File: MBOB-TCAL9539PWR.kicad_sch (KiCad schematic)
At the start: 1 part

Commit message: Finished drawing the schematics
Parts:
- added C1: 10u, symbol Device:C_Small
- added C2: 100n, symbol Device:C_Small
- added D1: LED, symbol Device:LED
- added H1, H2, H3, H4: MountingHole, symbol Mechanical:MountingHole
- added J1, J2: Conn_01x10, symbol Connector_Generic:Conn_01x10
- added J3, J4: QWIIC Right Angle, symbol Connector_Generic:Conn_01x04
- added J5: Conn_02x03_Odd_Even, symbol Connector_Generic:Conn_02x03_Odd_Even
- added JP1: SolderJumper_3_Open, symbol Jumper:SolderJumper_3_Open
- added JP2, JP3: SolderJumper_2_Open, symbol Jumper:SolderJumper_2_Open
- added R1, R2, R3, R4, R5, R6, R7: 4K7, symbol Device:R_Small
- U1: value ~ -> TCAL9539PWR; footprint (none) -> Package_SO:TSSOP-24_4.4x6.5mm_P0.5mm
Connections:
- net ~{INT}: now reaches U1.1 (~{INT})
- net ~{INT}: now also J5.5 (Pin_5), R2.2
- net P6: now reaches U1.10 (P6)
- net P6: now also J1.8 (Pin_8)
- net P7: now reaches U1.11 (P7)
- net P7: now also J1.9 (Pin_9)
- net P10: now reaches U1.13 (P10)
- net P10: now also J2.2 (Pin_2)
- net P11: now reaches U1.14 (P11)
- net P11: now also J2.3 (Pin_3)
- net P12: now reaches U1.15 (P12)
- net P12: now also J2.4 (Pin_4)
- net P13: now reaches U1.16 (P13)
- net P13: now also J2.5 (Pin_5)
- net P14: now reaches U1.17 (P14)
- net P14: now also J2.6 (Pin_6)
- net P15: now reaches U1.18 (P15)
- net P15: now also J2.7 (Pin_7)
- net P16: now reaches U1.19 (P16)
- net P16: now also J2.8 (Pin_8)
- net P17: now reaches U1.20 (P17)
- net P17: now also J2.9 (Pin_9)
- net SCL: now reaches U1.22 (SCL)
- net SCL: now also J3.4 (Pin_4), J4.4 (Pin_4), J5.3 (Pin_3), R4.2
- net SDA: now reaches U1.23 (SDA)
- net SDA: now also J3.3 (Pin_3), J4.3 (Pin_3), J5.1 (Pin_1), R3.2
- net +3.3V: now reaches U1.24 (VCC)
- net +3.3V: now also C1.1, C2.1, J1.1 (Pin_1), J2.1 (Pin_1), J3.2 (Pin_2), J4.2 (Pin_2), JP1.2 (C), JP2.2 (B), JP3.2 (B), R1.1, R2.1, R7.1
- net GND: now reaches U1.25 (GND)
- net GND: now also C1.2, C2.2, D1.1 (K), J1.10 (Pin_10), J2.10 (Pin_10), J3.1 (Pin_1), J4.1 (Pin_1), R5.2, R6.2
- net A0: now reaches U1.26 (A0)
- net A0: now also J5.4 (Pin_4), JP2.1 (A), R5.1
- net A1: now reaches U1.27 (A1)
- net A1: now also J5.6 (Pin_6), JP3.1 (A), R6.1
- net ~{RESET}: now reaches U1.3 (~{RESET})
- net ~{RESET}: now also J5.2 (Pin_2), R1.2
- net P0: now reaches U1.4 (P0)
- net P0: now also J1.2 (Pin_2)
- net P1: now reaches U1.5 (P1)
- net P1: now also J1.3 (Pin_3)
- net P2: now reaches U1.6 (P2)
- net P2: now also J1.4 (Pin_4)
- net P3: now reaches U1.7 (P3)
- net P3: now also J1.5 (Pin_5)
- net P4: now reaches U1.8 (P4)
- net P4: now also J1.6 (Pin_6)
- net P5: now reaches U1.9 (P5)
- net P5: now also J1.7 (Pin_7)
- new net: JP1.1 (A), R4.1
- new net: JP1.3 (B), R3.1
- new net: D1.2 (A), R7.2
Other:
- note added: "I2C Address Select"
- note added: "I2C address: [A1][A0] 00 - 0x74 (Default) 01 - 0x75 11 - 0x76 10 - 0x77"
- note added: "JP1 enables/disables 4K7 pull-up resistors on the SDA/SCL lines. (Default: Open)"
- note added: "JP2 and JP3 set the I2C address of the TCAL9539PWR"
- note added: "LED + Header"
- note added: "QWIIC Connectors + Mounting"
- note added: "QWIIC connector pinout pin 1: Black pin 2: Red pin 3: Blue pin 4: Yellow"
- note added: "TCAL9539PWR"

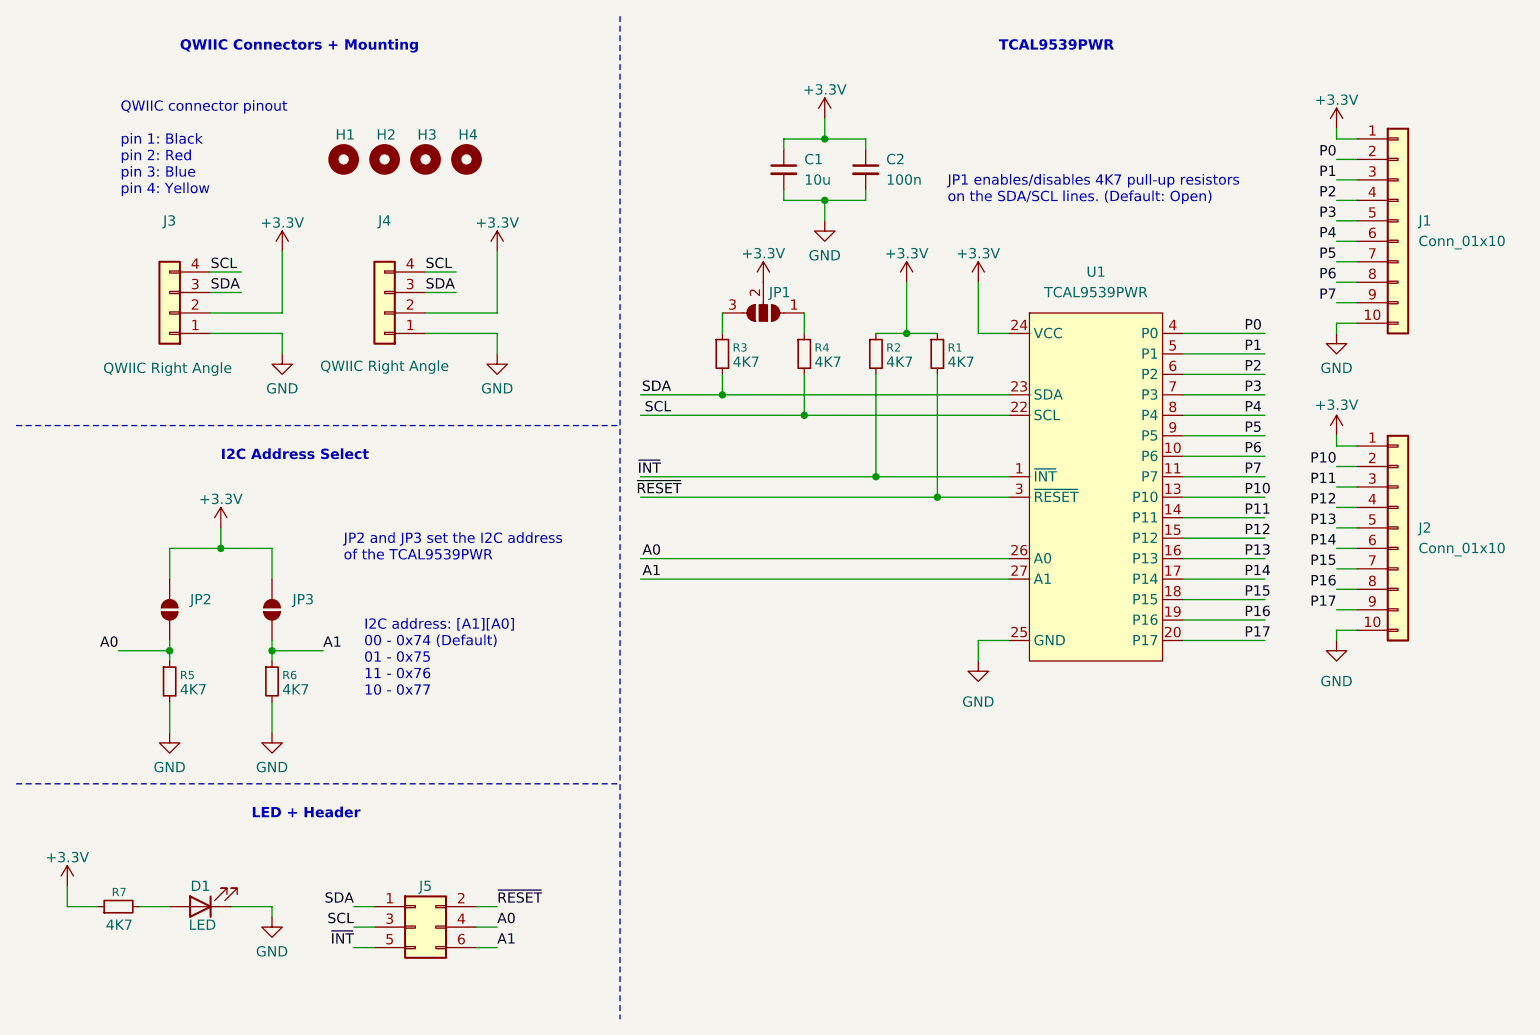
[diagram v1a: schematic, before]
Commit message: Added all the footprints
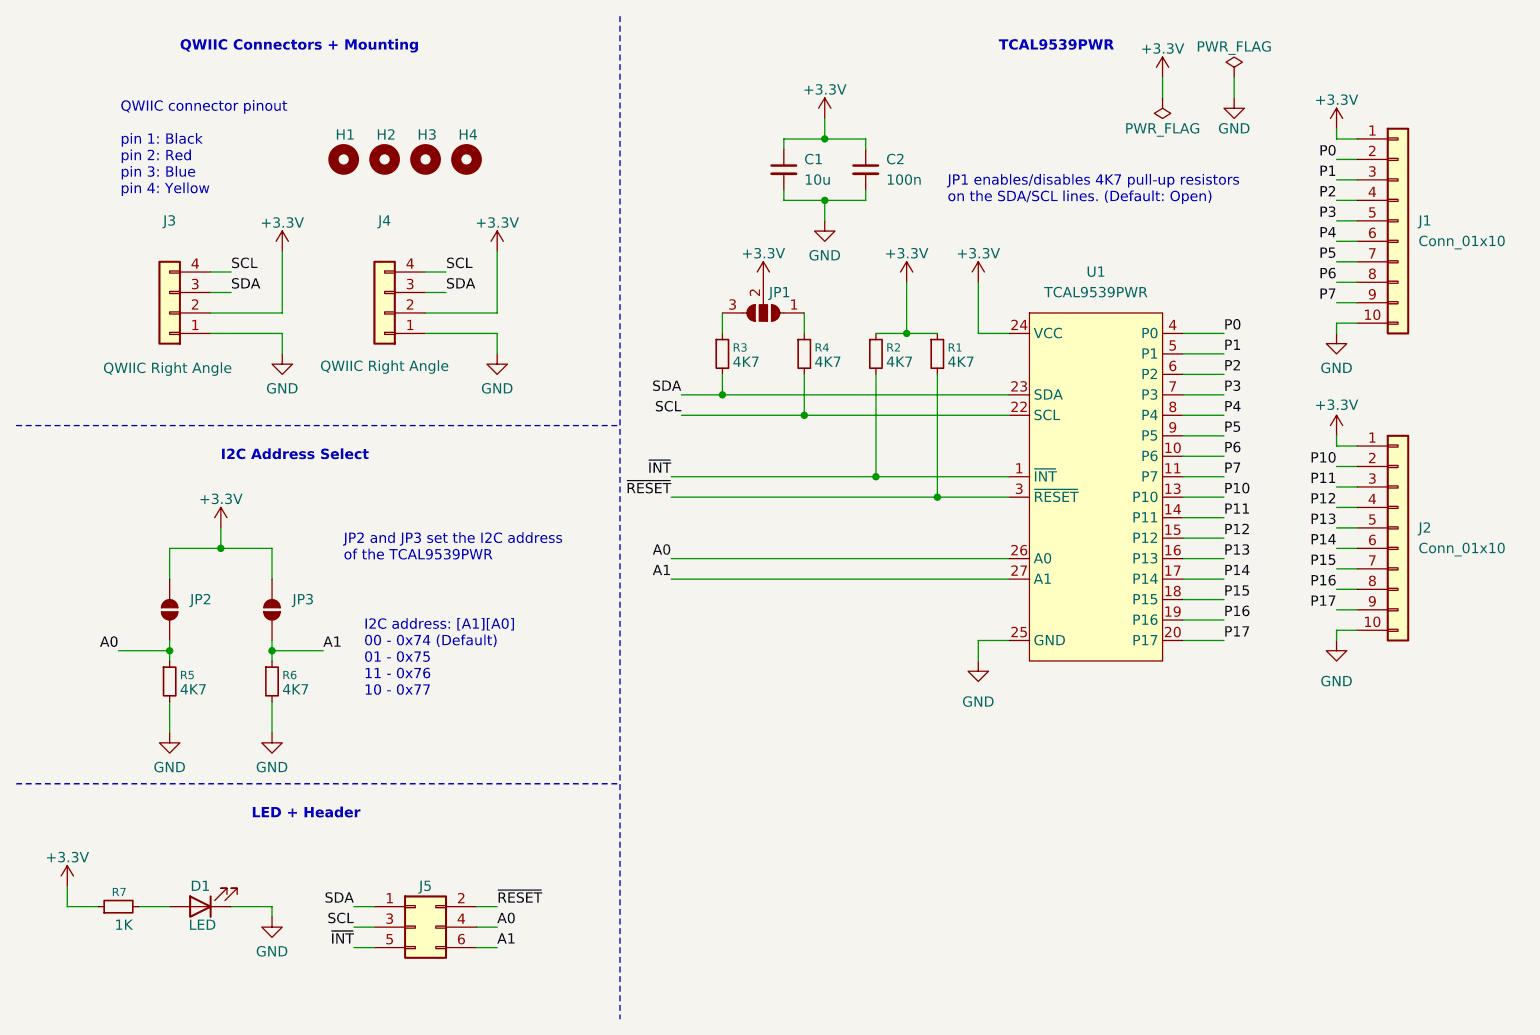
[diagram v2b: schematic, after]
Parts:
- C1: footprint (none) -> Capacitor_SMD:C_0603_1608Metric_Pad1.08x0.95mm_HandSolder
- C2: footprint (none) -> Capacitor_SMD:C_0402_1005Metric_Pad0.74x0.62mm_HandSolder
- D1: footprint (none) -> LED_SMD:LED_0603_1608Metric_Pad1.05x0.95mm_HandSolder
- H1, H2, H3, H4: footprint (none) -> MountingHole:MountingHole_3.2mm_M3_DIN965_Pad
- J1, J2: footprint (none) -> Connector_PinHeader_2.54mm:PinHeader_1x10_P2.54mm_Vertical
- J3, J4: footprint (none) -> Connector_JST:JST_SH_SM04B-SRSS-TB_1x04-1MP_P1.00mm_Horizontal
- J5: footprint (none) -> Connector_PinHeader_2.54mm:PinHeader_2x03_P2.54mm_Vertical
- JP1: footprint (none) -> Jumper:SolderJumper-3_P1.3mm_Open_RoundedPad1.0x1.5mm
- JP2, JP3: footprint (none) -> Jumper:SolderJumper-2_P1.3mm_Open_RoundedPad1.0x1.5mm
- R1, R2, R3, R4, R5, R6: footprint (none) -> Resistor_SMD:R_0402_1005Metric_Pad0.72x0.64mm_HandSolder
- R7: value 4K7 -> 1K; footprint (none) -> Resistor_SMD:R_0402_1005Metric_Pad0.72x0.64mm_HandSolder

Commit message: Final commit
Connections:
- net A0: now also U1.21 (A0); no longer U1.26 (A0)
- net A1: now also U1.2 (A1); no longer U1.27 (A1)
- net GND: now also U1.12 (GND); no longer U1.25 (GND)
- net P10: now also J2.9 (Pin_9); no longer J2.2 (Pin_2)
- net P11: now also J2.8 (Pin_8); no longer J2.3 (Pin_3)
- net P12: now also J2.7 (Pin_7); no longer J2.4 (Pin_4)
- net P13: now also J2.6 (Pin_6); no longer J2.5 (Pin_5)
- net P14: now also J2.5 (Pin_5); no longer J2.6 (Pin_6)
- net P15: now also J2.4 (Pin_4); no longer J2.7 (Pin_7)
- net P16: now also J2.3 (Pin_3); no longer J2.8 (Pin_8)
- net P17: now also J2.2 (Pin_2); no longer J2.9 (Pin_9)
